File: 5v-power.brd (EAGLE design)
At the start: 85.7 x 34.6 mm, 29 parts, among them IC1 LM2576, J1 Bypass, J2 En, J3 12v, J4 5V Out, J5 LEN EN, Q1 SI4532ADY

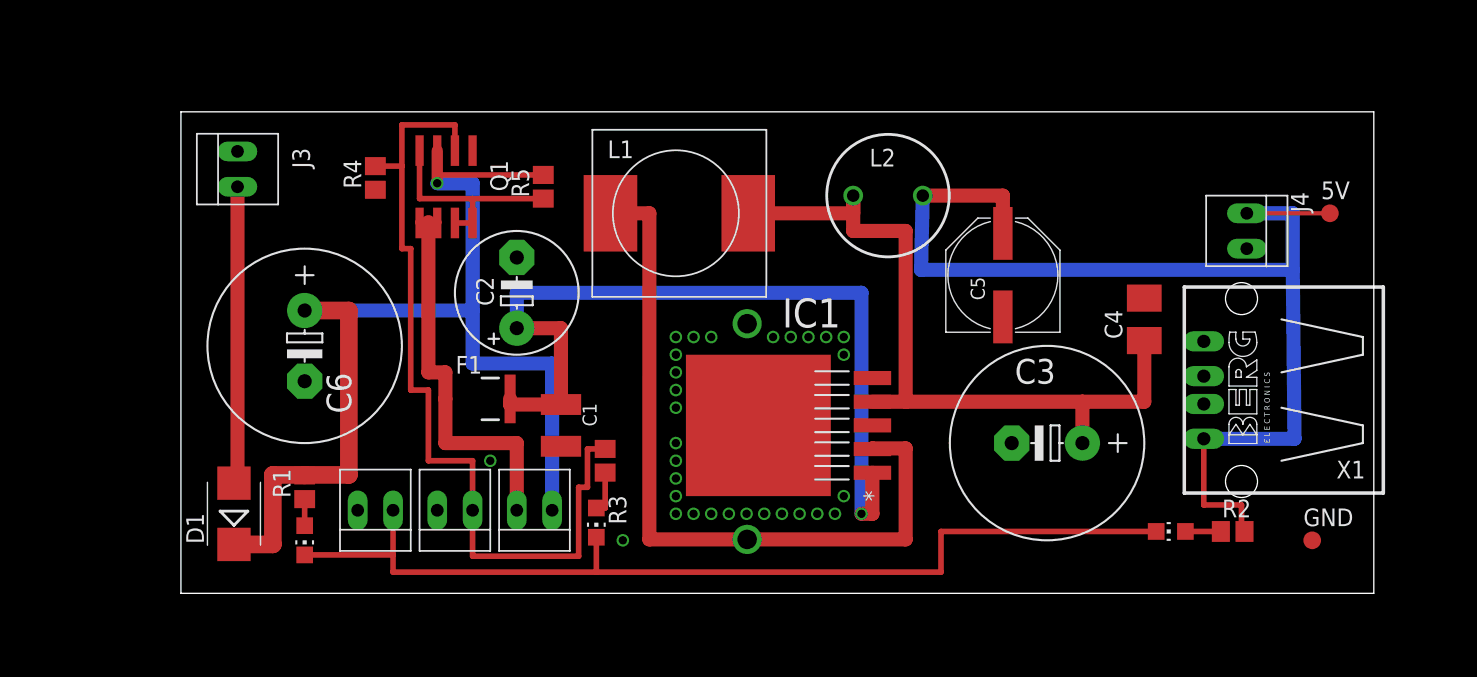
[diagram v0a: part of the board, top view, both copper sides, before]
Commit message: power pole in and out now added
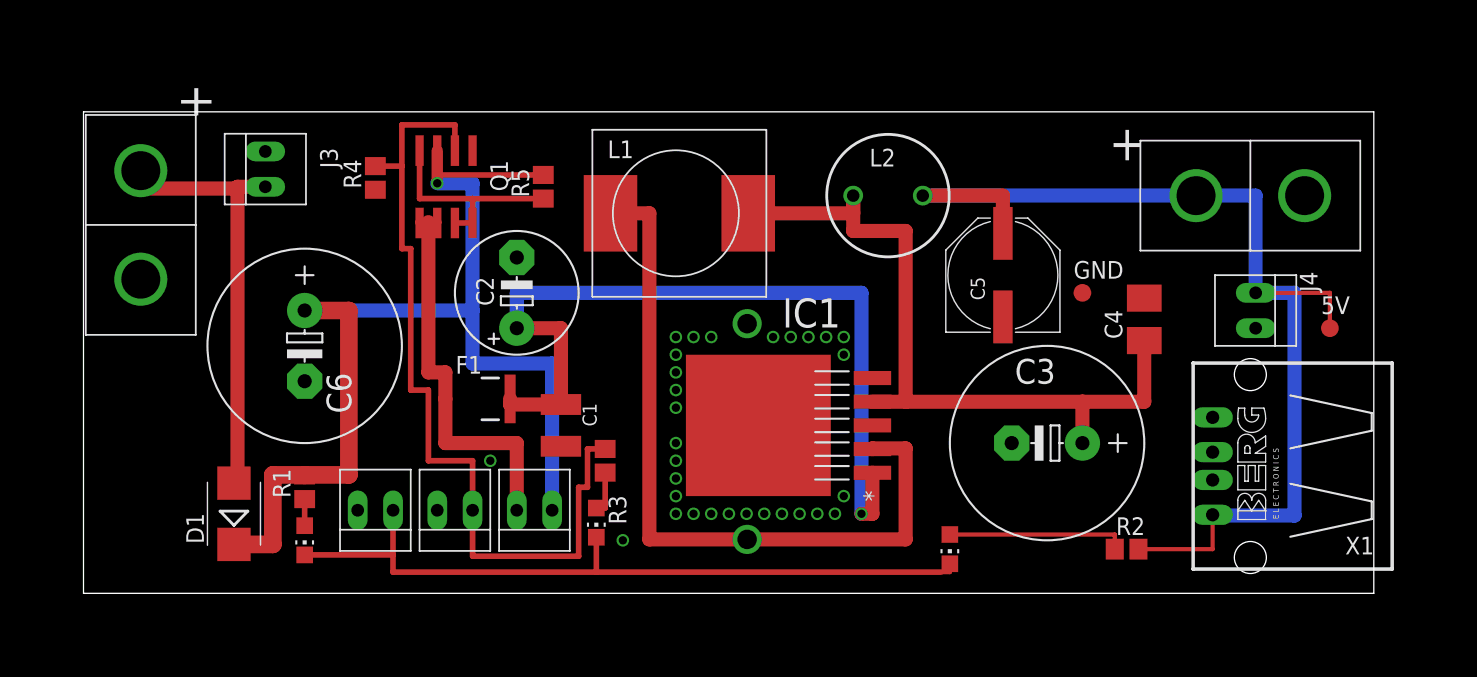
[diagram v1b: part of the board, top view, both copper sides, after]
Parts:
- added J6, J7: POWERPOLE_POWER10AWG, powerpoles:POWERPOLE_PAIR_10AWG
- moved GND 24.3 mm to (94.0, 54.0)
- moved LED2 15.9 mm to (84.5, 35.6), turned to 180 degrees
- moved 5V 8.25 mm to (111.8, 51.4)
- moved R2 7.73 mm to (97.2, 35.6)
- moved J4 5.75 mm to (106.0, 52.7)
- moved X1 5.50 mm to (106.0, 41.5)
- moved J3 2.00 mm to (35.7, 62.9)
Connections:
- net 5V: now also J6.RED
- net GND: now also J6.BLACK, J7.BLACK
- net N$1: now also J7.RED
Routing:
- net LEDGND: track 71.1 -> 53.9 mm
- net N$47: track 2.55 -> 12.9 mm
- net N$1: track 21.5 -> 31.8 mm
- net 5V: track 82.5 -> 79.8 mm
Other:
- board size 85.7 x 34.6 mm -> 92.7 x 34.6 mm
- board text added: "Version 0.2"
- board text removed: "Version 0.1"
